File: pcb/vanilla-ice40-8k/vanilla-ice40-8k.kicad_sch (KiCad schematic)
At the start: 17 parts, among them J1 QSH-060-01-L-D-A, J2 QSH-060-01-L-D-A, J3 QTH-060-01-L-D-A, J4 QTH-060-01-L-D-A, U1 ICE40HX8K-CT256, X1 SG-8101CE 100Mhz

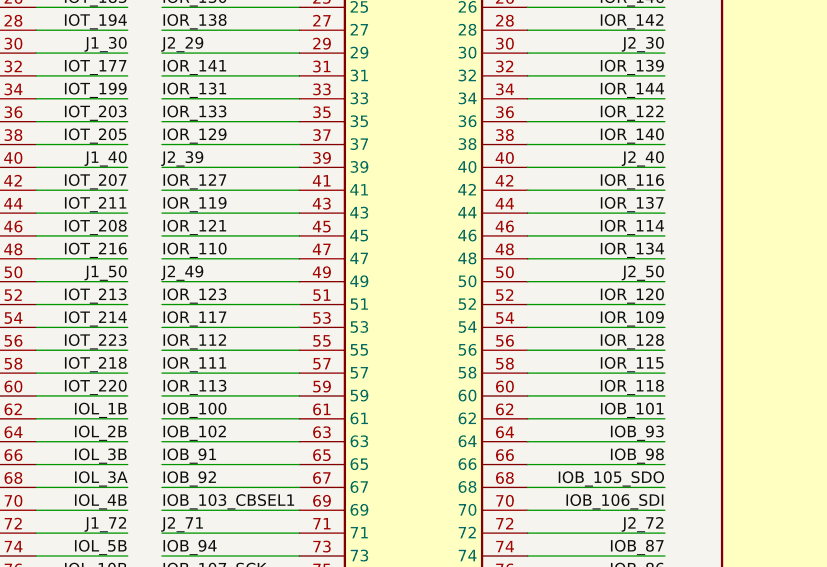
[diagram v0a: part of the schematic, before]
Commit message: [hx8k][pcb] upper j2 sig4 routed
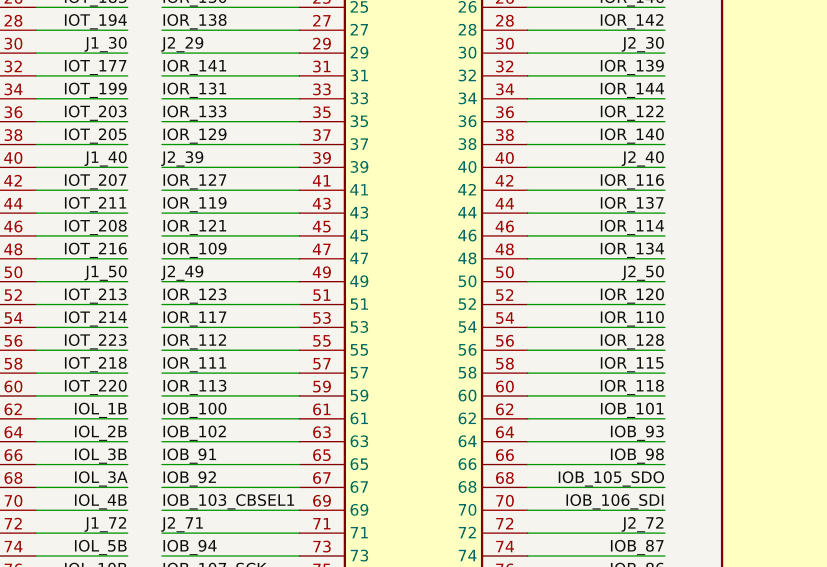
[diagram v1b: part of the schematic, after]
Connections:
- net IOR_109: now also J4.47; no longer J4.54
- net IOR_110: now also J4.54; no longer J4.47
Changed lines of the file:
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@@
 	)
 	(label "IOR_110"
-		(at 172.72 154.94 0)
-		(effects
-			(font
-				(size 1.27 1.27)
-			)
-			(justify left bottom)
+		(at 228.6 162.56 180)
+		(effects
+			(font
+				(size 1.27 1.27)
+			)
+			(justify right bottom)
 		)
 	)
@@
 	)
 	(label "IOR_109"
-		(at 228.6 162.56 180)
-		(effects
-			(font
-				(size 1.27 1.27)
-			)
-			(justify right bottom)
-		)
-	)
+		(at 172.72 154.94 0)
+		(effects
+			(font
+				(size 1.27 1.27)
+			)
+			(justify left bottom)
+		)
+	)

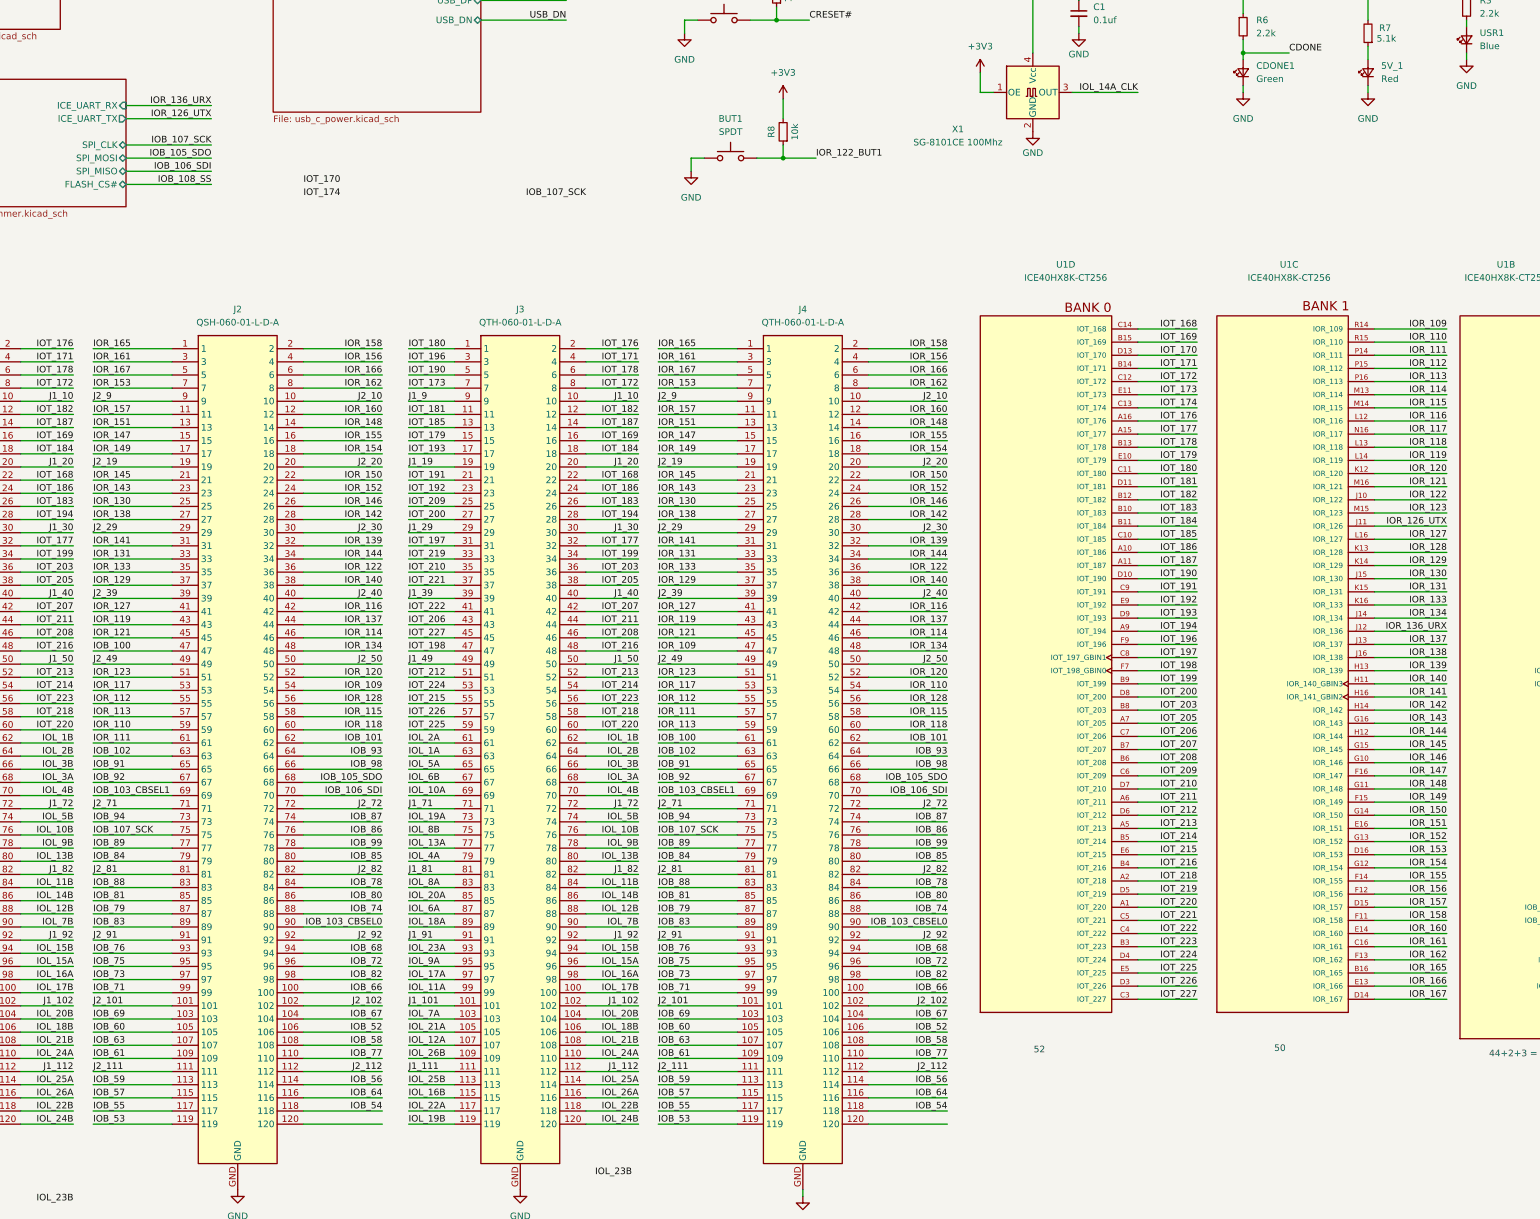
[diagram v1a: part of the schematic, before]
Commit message: [hx8k][pcb] upper j2 routed, passes drc
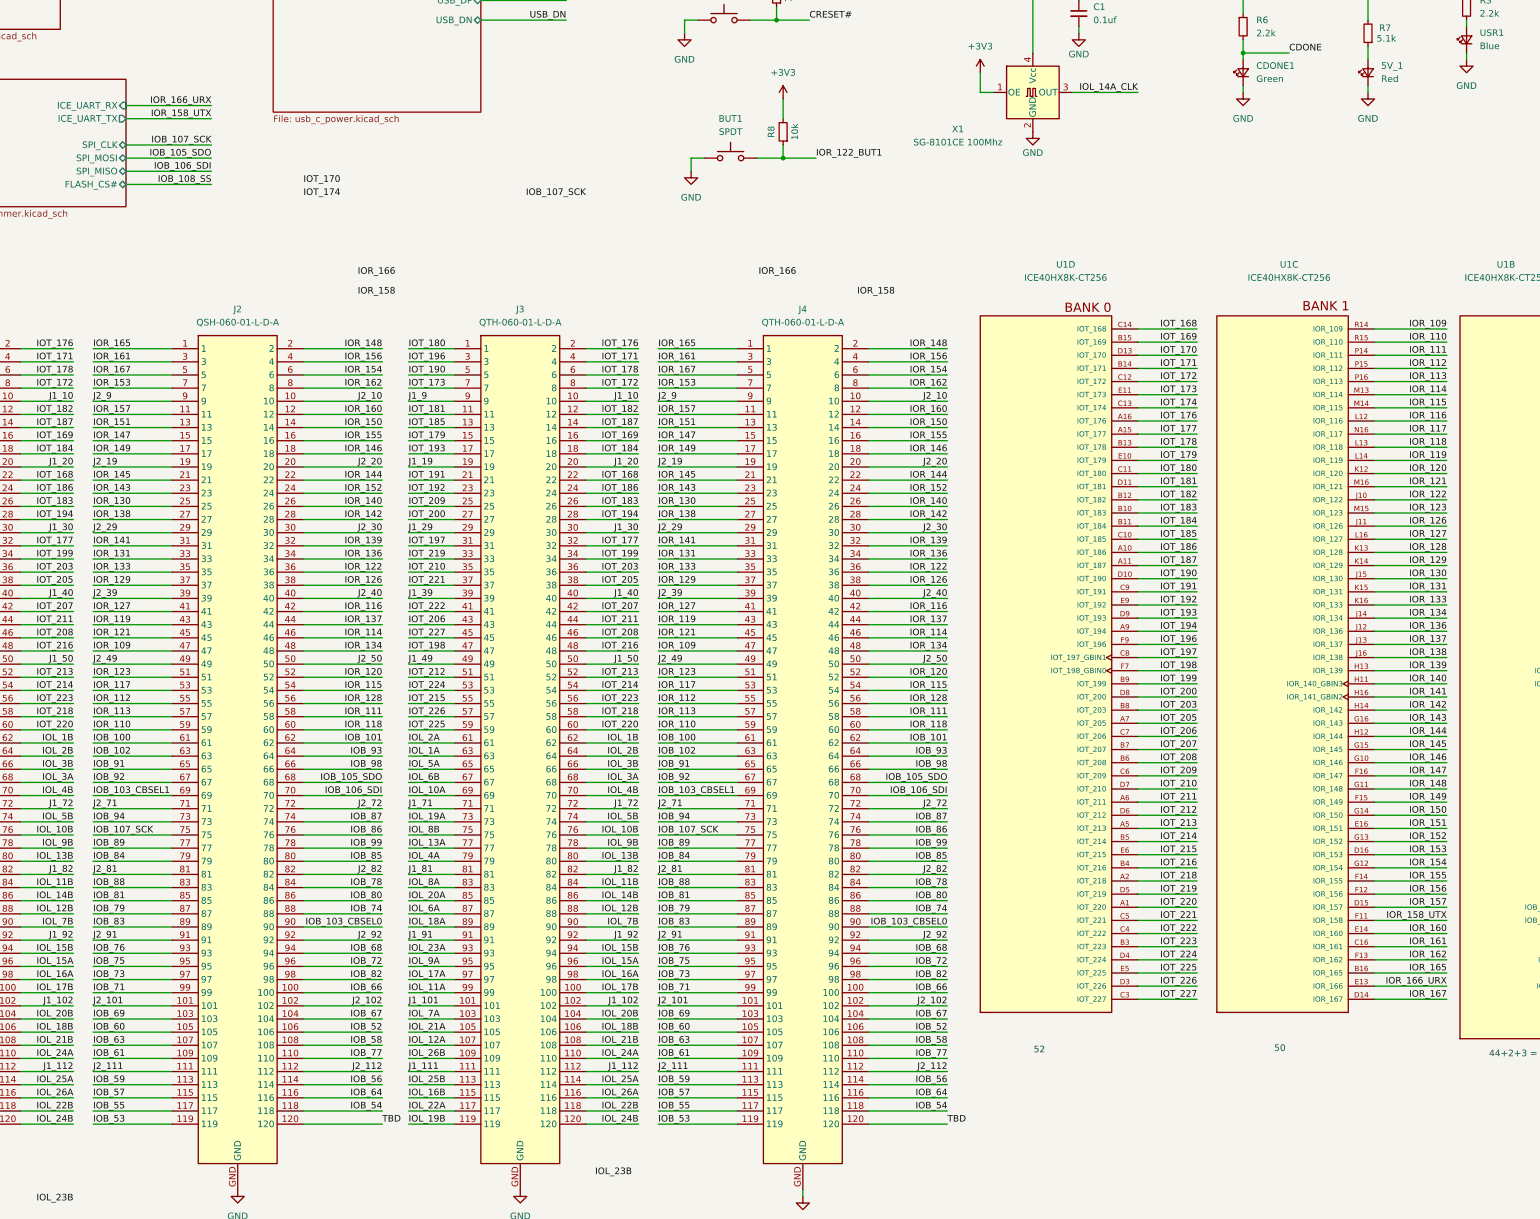
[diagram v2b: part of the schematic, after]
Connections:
- net IOB_100: now also J2.61; no longer J2.47
- net IOR_109: now also J2.47; no longer J2.54
- net IOR_110: now also J4.59; no longer J4.54
- net IOR_111: now also J2.58, J4.58; no longer J2.61, J4.57
- net IOR_113: now also J4.57; no longer J4.59
- net IOR_115: now also J2.54, J4.54; no longer J2.58, J4.58
- net IOR_140: now also J2.26, J4.26; no longer J2.38, J4.38
- net IOR_144: now also J2.22, J4.22; no longer J2.34, J4.34
- net IOR_146: now also J2.18, J4.18; no longer J2.26, J4.26
- net IOR_148: now also J2.2, J4.2; no longer J2.14, J4.14
- net IOR_150: now also J2.14, J4.14; no longer J2.22, J4.22
- net IOR_154: now also J2.6, J4.6; no longer J2.18, J4.18
- net IOR_158: no longer J2.2, J4.2, U1.F11 (IOR_158)
- net IOR_166: no longer J2.6, J4.6, U1.E13 (IOR_166)
- net TBD: now reaches J4.120
- net TBD: now also J2.120
- net IOR_126_UTX renamed IOR_126
- net IOR_126: now also J2.38, J4.38
- net IOR_136_URX renamed IOR_136
- net IOR_136: now also J2.34, J4.34
- new net IOR_158_UTX: U1.F11 (IOR_158)
- new net IOR_166_URX: U1.E13 (IOR_166)

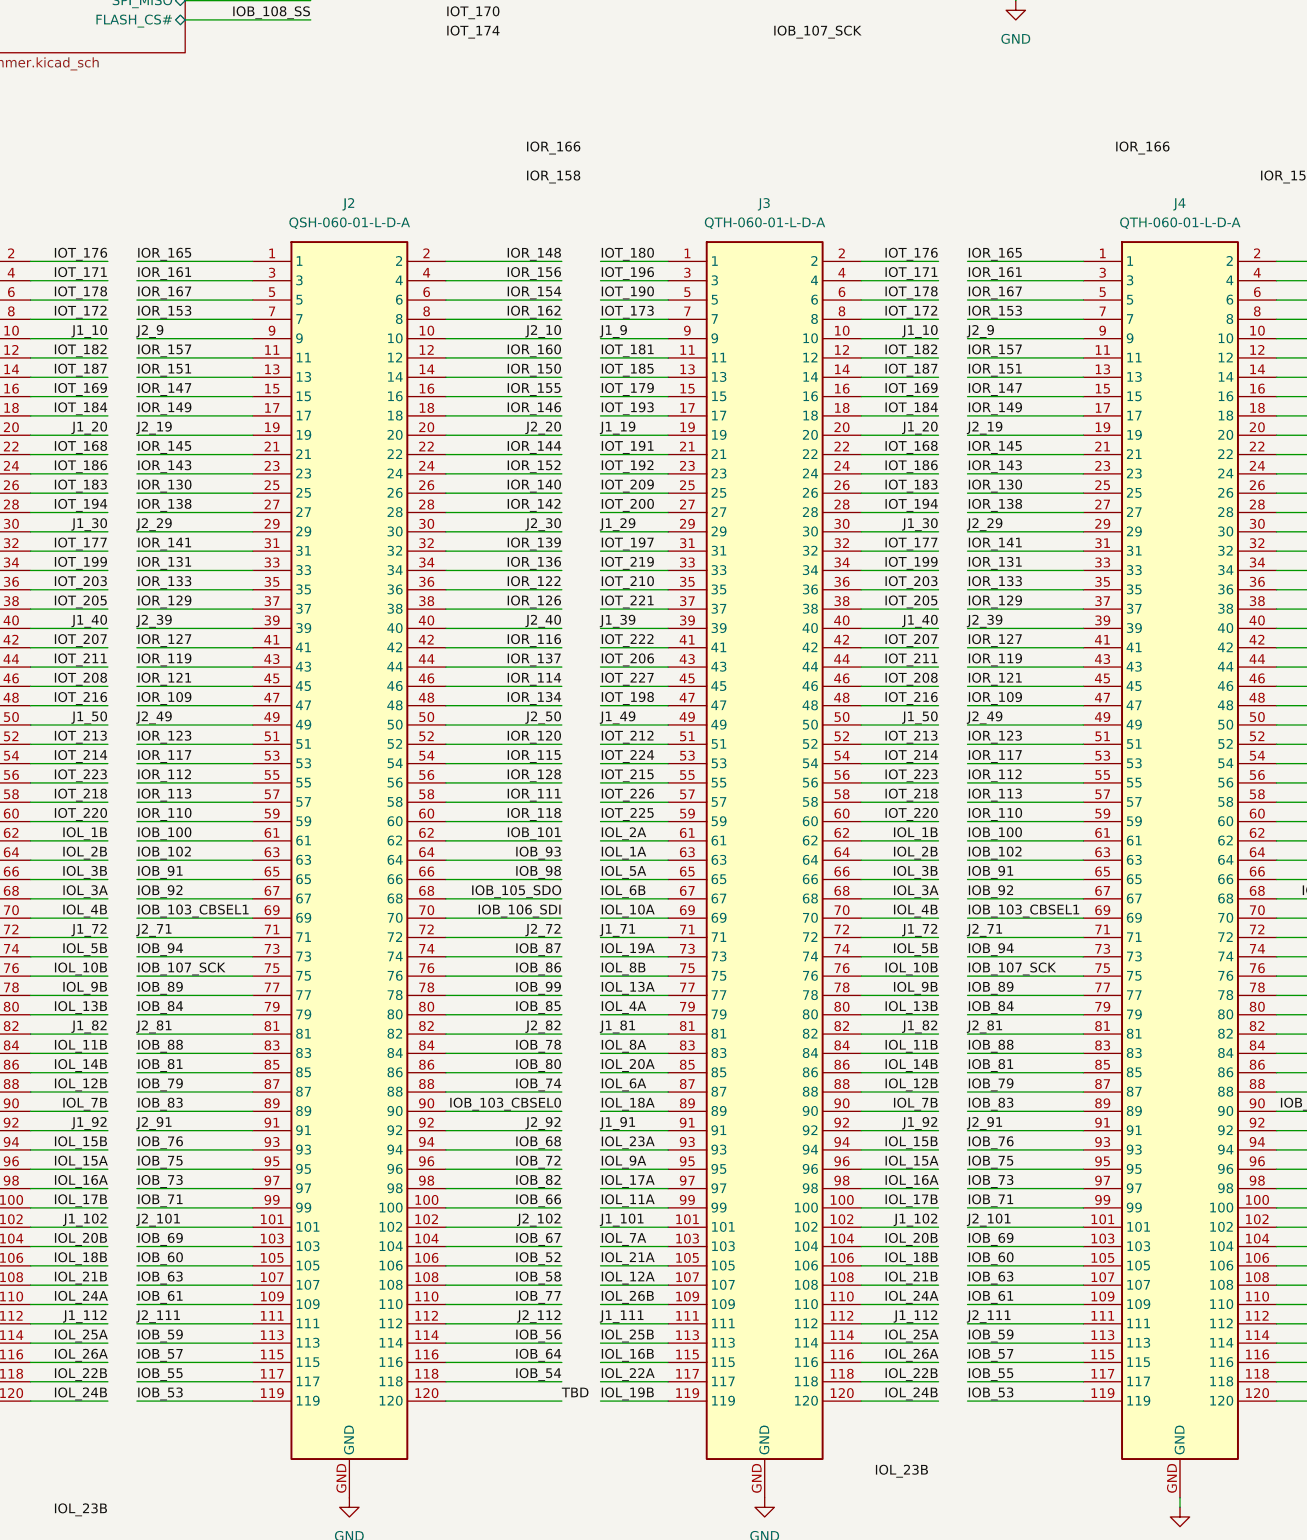
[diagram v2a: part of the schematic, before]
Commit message: [hx8k][pcb] lower j2 l1 routed
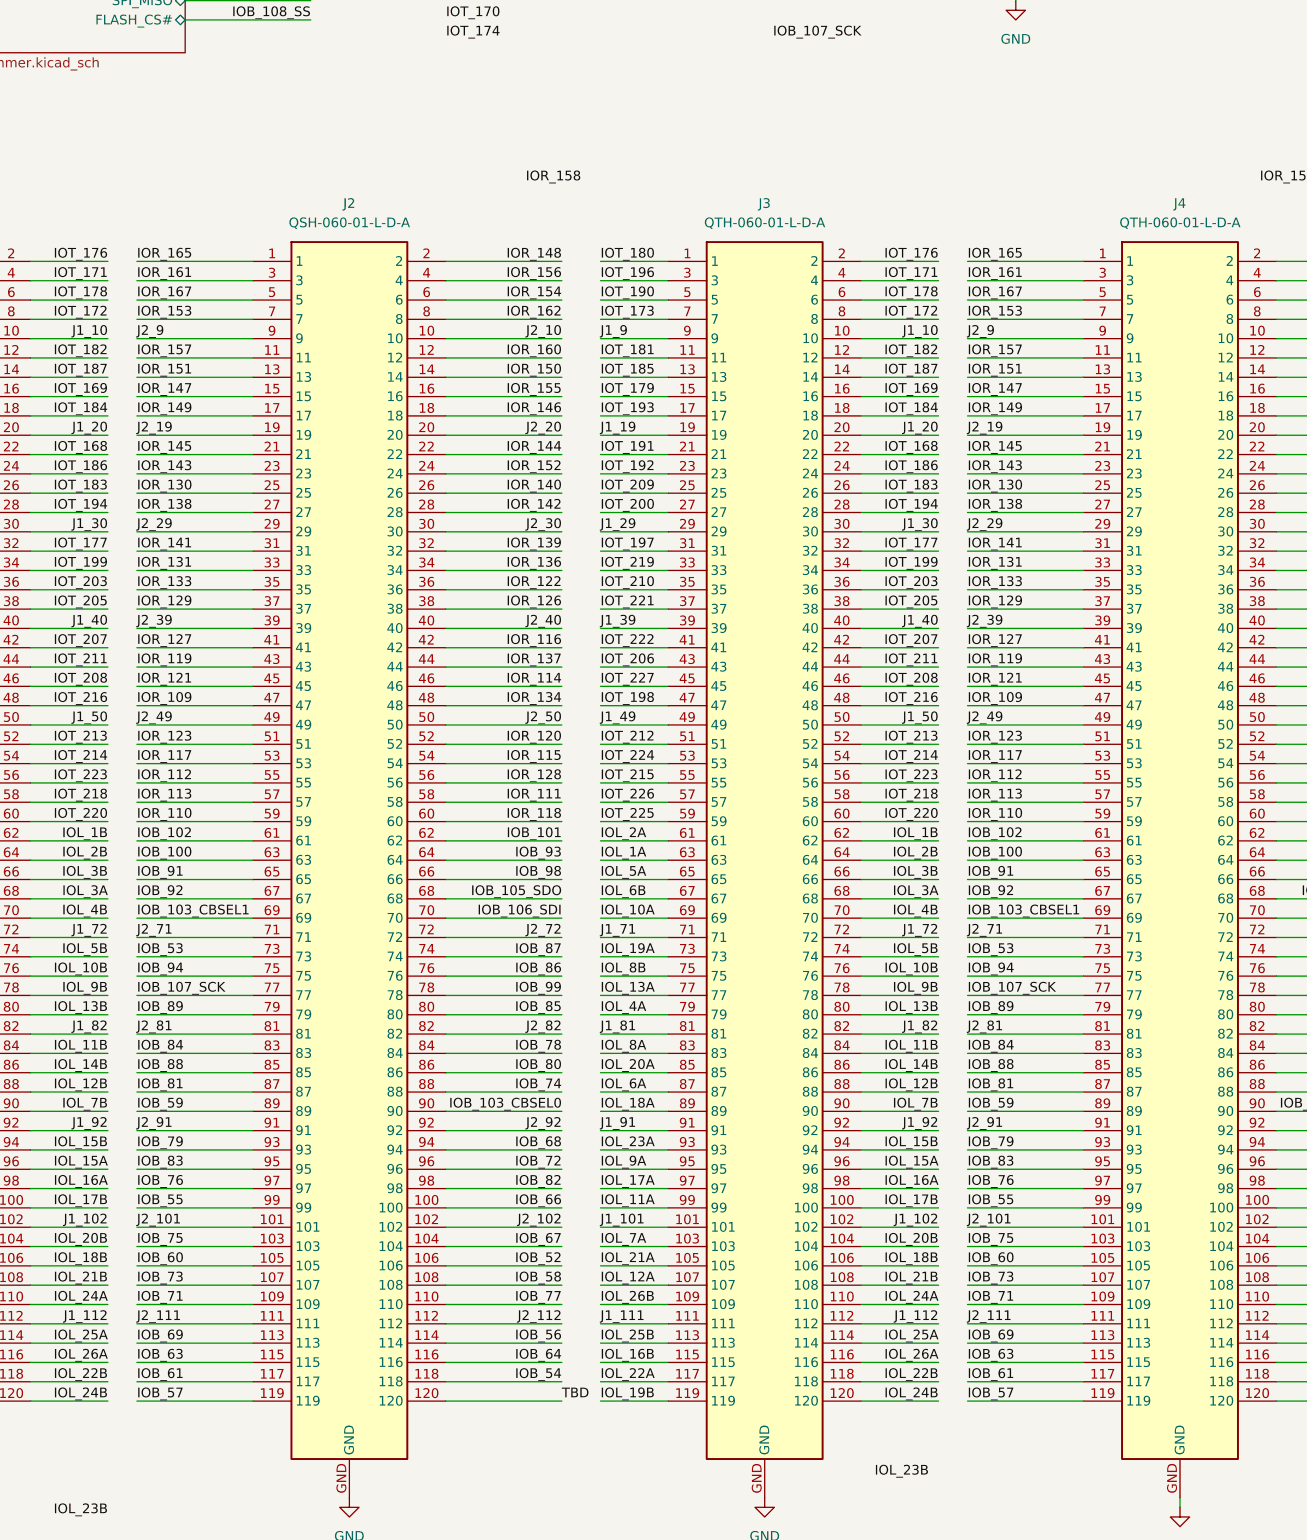
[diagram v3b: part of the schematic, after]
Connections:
- net IOB_100: now also J2.63, J4.63; no longer J2.61, J4.61
- net IOB_102: now also J2.61, J4.61; no longer J2.63, J4.63
- net IOB_107_SCK: now also J2.77, J4.77; no longer J2.75, J4.75
- net IOB_53: now also J2.73, J4.73; no longer J2.119, J4.119
- net IOB_55: now also J2.99, J4.99; no longer J2.117, J4.117
- net IOB_57: now also J2.119, J4.119; no longer J2.115, J4.115
- net IOB_59: now also J2.89, J4.89; no longer J2.113, J4.113
- net IOB_61: now also J2.117, J4.117; no longer J2.109, J4.109
- net IOB_63: now also J2.115, J4.115; no longer J2.107, J4.107
- net IOB_69: now also J2.113, J4.113; no longer J2.103, J4.103
- net IOB_71: now also J2.109, J4.109; no longer J2.99, J4.99
- net IOB_73: now also J2.107, J4.107; no longer J2.97, J4.97
- net IOB_75: now also J2.103, J4.103; no longer J2.95, J4.95
- net IOB_76: now also J2.97, J4.97; no longer J2.93, J4.93
- net IOB_79: now also J2.93, J4.93; no longer J2.87, J4.87
- net IOB_81: now also J2.87, J4.87; no longer J2.85, J4.85
- net IOB_83: now also J2.95, J4.95; no longer J2.89, J4.89
- net IOB_84: now also J2.83, J4.83; no longer J2.79, J4.79
- net IOB_88: now also J2.85, J4.85; no longer J2.83, J4.83
- net IOB_89: now also J2.79, J4.79; no longer J2.77, J4.77
- net IOB_94: now also J2.75, J4.75; no longer J2.73, J4.73
